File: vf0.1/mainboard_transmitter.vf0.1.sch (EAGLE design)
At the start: 10 parts, among them J1 AUDIO-JACK2PTH, Y1 16MHz

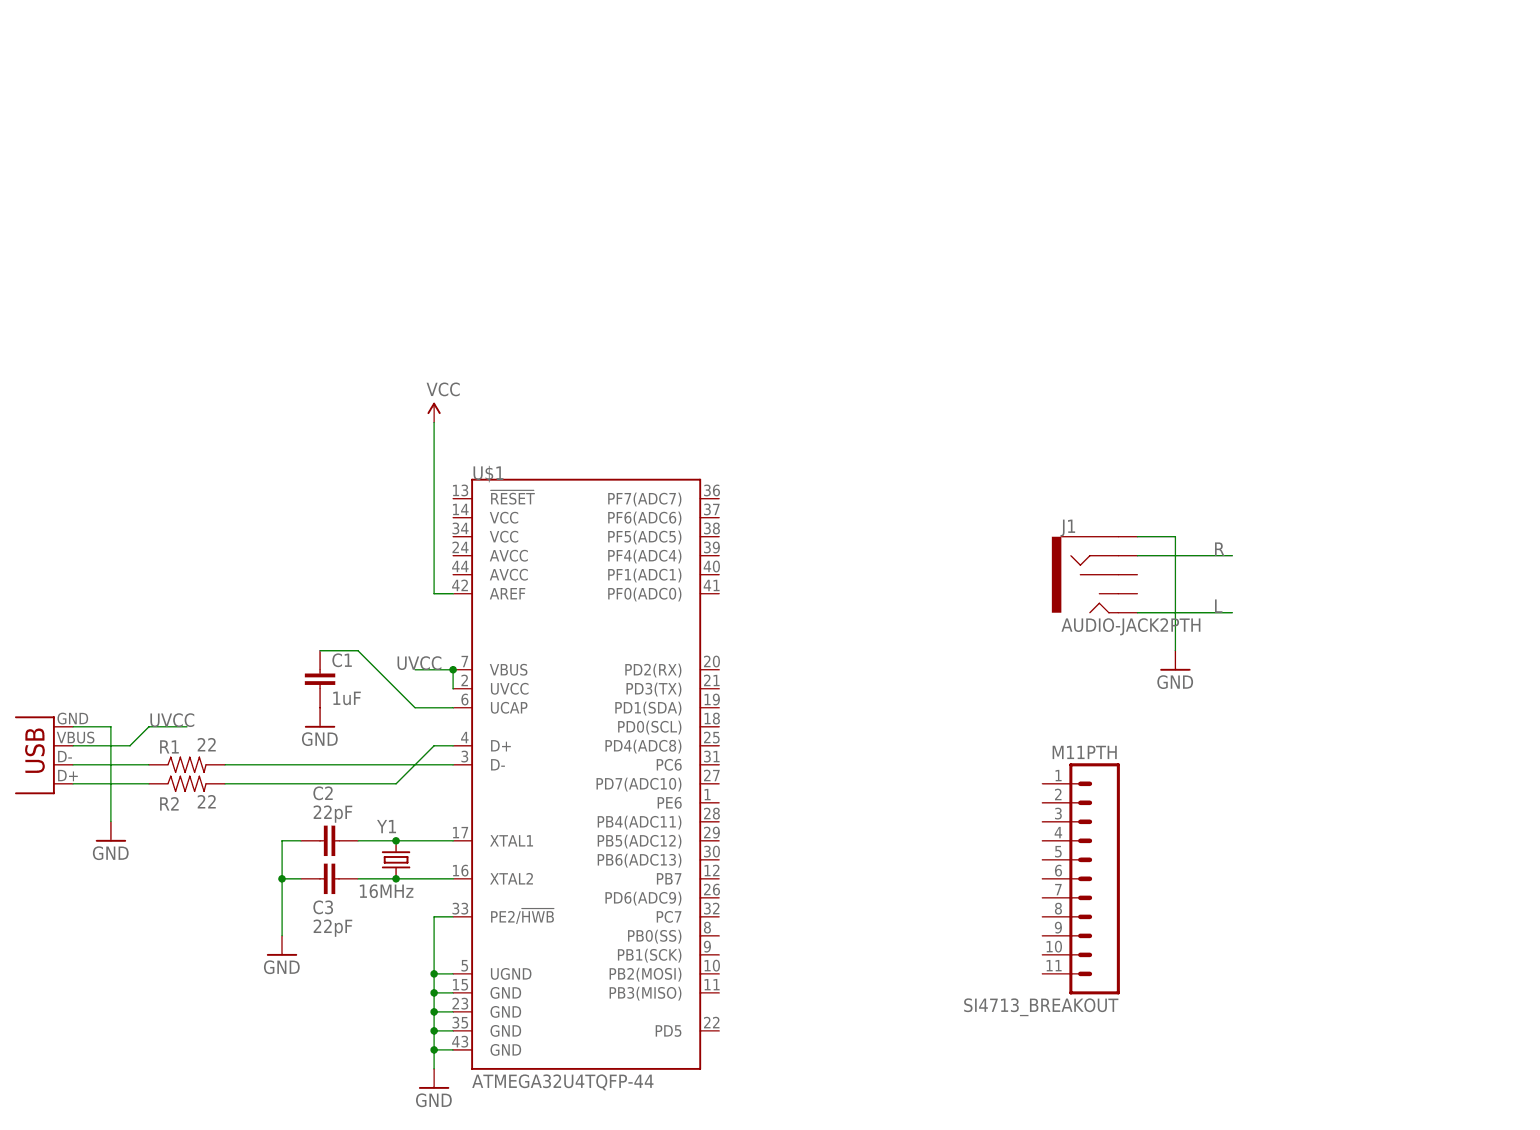
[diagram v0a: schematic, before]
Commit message: Mostly complete, routed audio, FM transmitter, data transmitter
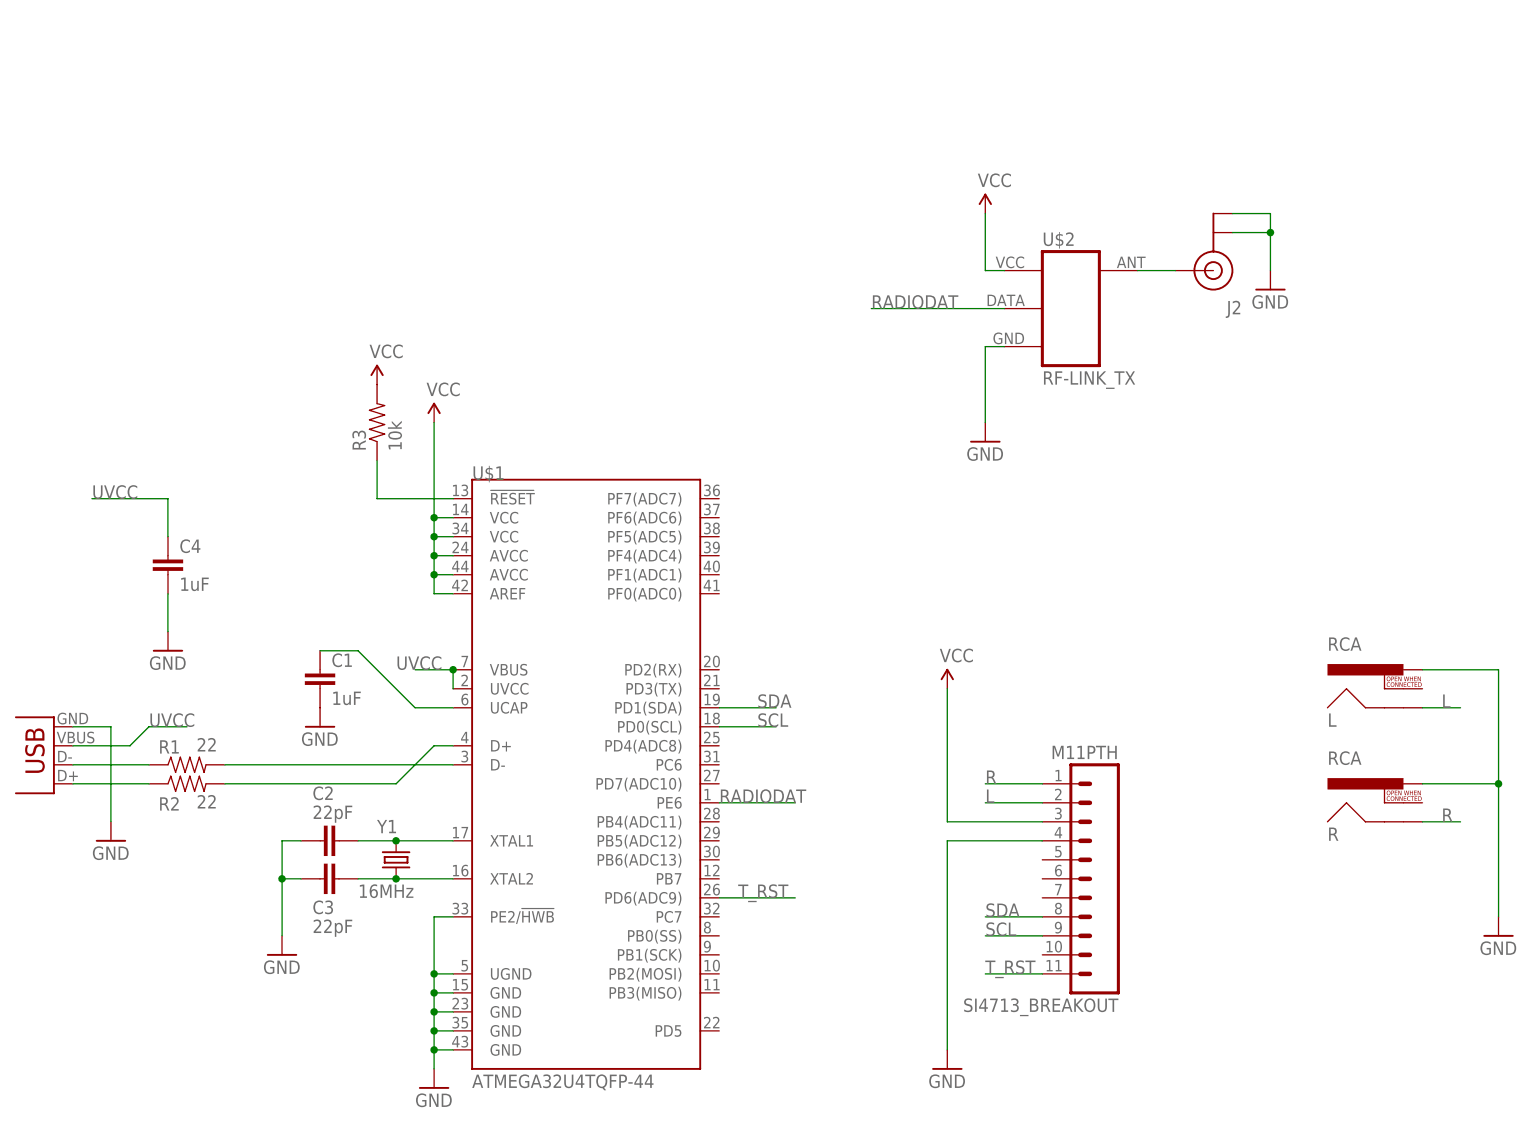
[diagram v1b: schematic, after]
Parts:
- removed J1: AUDIO-JACK2PTH, SparkFun-Connectors:AUDIO-JACK2PTH
- added C4: 1uF, SparkFun-Capacitors:CAPPTH
- added J2: U.FL, SparkFun-Connectors:U.FL
- added L, R: RCA, SparkFun-Connectors:RCA
- added R3: 10k, SparkFun-Resistors:10KOHM-1/4W5%(PTH)VERT
- added U$2: RF-LINK_TX, SparkFun-RF:RF-LINK_TX
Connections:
- new net N$8: R3.1, U$1.!RESET
- new net N$9: J2.SIGNAL, U$2.ANT
- new net RADIODAT: U$1.PE6, U$2.DATA
- new net SCL: SI4713_BREAKOUT.9, U$1.PD0(SCL)
- new net SDA: SI4713_BREAKOUT.8, U$1.PD1(SDA)
- new net T_RST: SI4713_BREAKOUT.11, U$1.PD6(ADC9)
- net GND: now also C4.2, J2.GND@0, J2.GND@1, L.PIN, R.PIN, SI4713_BREAKOUT.4, U$2.GND; no longer J1.SLEEVE
- net L: now also L.SHELL, SI4713_BREAKOUT.2; no longer J1.TIP
- net R: now also R.SHELL, SI4713_BREAKOUT.1; no longer J1.RING
- net UVCC: now also C4.1
- net VCC: now also R3.2, SI4713_BREAKOUT.3, U$1.AVCC@24, U$1.AVCC@44, U$1.VCC@14, U$1.VCC@34, U$2.+5V

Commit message: Final revision of vf0.1
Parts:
- removed J2: U.FL, SparkFun-Connectors:U.FL
- added J$1: SMA_EDGE, SparkFun-Connectors:SMA_EDGE
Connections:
- removed net UVCC: C4.1, JP1.VBUS, U$1.UVCC, U$1.VBUS
- net GND: now also J$1.GND@0, J$1.GND@1, J$1.GND@2, J$1.GND@3; no longer J2.GND@0, J2.GND@1
- net N$9: now also J$1.SIGNAL; no longer J2.SIGNAL
- net VCC: now also C4.1, JP1.VBUS, U$1.UVCC, U$1.VBUS
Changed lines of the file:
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@@
 <part name="R" library="SparkFun-Connectors" deviceset="RCA" device=""/>
 <part name="GND6" library="SparkFun-Aesthetics" deviceset="GND" device=""/>
-<part name="J2" library="SparkFun-Connectors" deviceset="U.FL" device="" value="U.FL"/>
 <part name="GND8" library="SparkFun-Aesthetics" deviceset="GND" device=""/>
 <part name="U$2" library="SparkFun-RF" deviceset="RF-LINK_TX" device=""/>
@@
 <part name="C4" library="SparkFun-Capacitors" deviceset="CAP" device="PTH" value="1uF"/>
 <part name="GND9" library="SparkFun-Aesthetics" deviceset="GND" device=""/>
+<part name="SUPPLY5" library="SparkFun-Aesthetics" deviceset="VCC" device=""/>
+<part name="SUPPLY6" library="SparkFun-Aesthetics" deviceset="VCC" device=""/>
+<part name="SUPPLY7" library="SparkFun-Aesthetics" deviceset="VCC" device=""/>
+<part name="J$1" library="SparkFun-Connectors" deviceset="SMA_EDGE" device=""/>
 </parts>
 <sheets>
@@
 <instance part="R" gate="G$1" x="152.4" y="48.26"/>
 <instance part="GND6" gate="1" x="162.56" y="30.48"/>
-<instance part="J2" gate="G$1" x="124.46" y="119.38" rot="R180"/>
 <instance part="GND8" gate="1" x="132.08" y="116.84"/>
 <instance part="U$2" gate="G$1" x="104.14" y="116.84"/>
@@
 <instance part="C4" gate="G$1" x="-15.24" y="78.74"/>
 <instance part="GND9" gate="1" x="-15.24" y="68.58"/>
+<instance part="SUPPLY5" gate="G$1" x="-20.32" y="58.42"/>
+<instance part="SUPPLY6" gate="G$1" x="-15.24" y="88.9"/>
+<instance part="SUPPLY7" gate="G$1" x="17.78" y="68.58"/>
+<instance part="J$1" gate="1" x="124.46" y="119.38" rot="R180"/>
 </instances>
 <busses>
@@
 </segment>
 <segment>
-<pinref part="J2" gate="G$1" pin="GND@1"/>
 <pinref part="GND8" gate="1" pin="GND"/>
 <wire x1="127" y1="127" x2="132.08" y2="127" width="0.1524" layer="91"/>
 <wire x1="132.08" y1="127" x2="132.08" y2="124.46" width="0.1524" layer="91"/>
-<pinref part="J2" gate="G$1" pin="GND@0"/>
 <wire x1="132.08" y1="124.46" x2="132.08" y2="119.38" width="0.1524" layer="91"/>
 <wire x1="127" y1="124.46" x2="132.08" y2="124.46" width="0.1524" layer="91"/>
 <junction x="132.08" y="124.46"/>
+<pinref part="J$1" gate="1" pin="GND@0"/>
+<pinref part="J$1" gate="1" pin="GND@1"/>
+<pinref part="J$1" gate="1" pin="GND@3"/>
+<wire x1="127" y1="132.08" x2="132.08" y2="132.08" width="0.1524" layer="91"/>
+<wire x1="132.08" y1="132.08" x2="132.08" y2="129.54" width="0.1524" layer="91"/>
+<junction x="132.08" y="127"/>
+<pinref part="J$1" gate="1" pin="GND@2"/>
+<wire x1="132.08" y1="129.54" x2="132.08" y2="127" width="0.1524" layer="91"/>
+<wire x1="127" y1="129.54" x2="132.08" y2="129.54" width="0.1524" layer="91"/>
+<junction x="132.08" y="129.54"/>
 </segment>
 <segment>
@@
 <wire x1="20.32" y1="55.88" x2="22.86" y2="55.88" width="0.1524" layer="91"/>
 <pinref part="U$1" gate="G$1" pin="D+"/>
-</segment>
-</net>
-<net name="UVCC" class="0">
-<segment>
-<pinref part="JP1" gate="G$1" pin="VBUS"/>
-<wire x1="-27.94" y1="55.88" x2="-20.32" y2="55.88" width="0.1524" layer="91"/>
-<wire x1="-20.32" y1="55.88" x2="-17.78" y2="58.42" width="0.1524" layer="91"/>
-<wire x1="-17.78" y1="58.42" x2="-12.7" y2="58.42" width="0.1524" layer="91"/>
-<label x="-17.78" y="58.42" size="1.778" layer="95"/>
-</segment>
-<segment>
-<pinref part="U$1" gate="G$1" pin="UVCC"/>
-<pinref part="U$1" gate="G$1" pin="VBUS"/>
-<wire x1="22.86" y1="66.04" x2="22.86" y2="63.5" width="0.1524" layer="91"/>
-<wire x1="22.86" y1="66.04" x2="17.78" y2="66.04" width="0.1524" layer="91"/>
-<junction x="22.86" y="66.04"/>
-<label x="15.24" y="66.04" size="1.778" layer="95"/>
-</segment>
-<segment>
-<pinref part="C4" gate="G$1" pin="1"/>
-<wire x1="-15.24" y1="83.82" x2="-15.24" y2="88.9" width="0.1524" layer="91"/>
-<wire x1="-15.24" y1="88.9" x2="-25.4" y2="88.9" width="0.1524" layer="91"/>
-<label x="-25.4" y="88.9" size="1.778" layer="95"/>
 </segment>
 </net>
@@
 <net name="N$9" class="0">
 <segment>
-<pinref part="J2" gate="G$1" pin="SIGNAL"/>
 <pinref part="U$2" gate="G$1" pin="ANT"/>
 <wire x1="119.38" y1="119.38" x2="114.3" y2="119.38" width="0.1524" layer="91"/>
+<pinref part="J$1" gate="1" pin="SIGNAL"/>
 </segment>
 </net>
@@
 <pinref part="SUPPLY4" gate="G$1" pin="VCC"/>
 </segment>
+<segment>
+<pinref part="JP1" gate="G$1" pin="VBUS"/>
+<wire x1="-27.94" y1="55.88" x2="-20.32" y2="55.88" width="0.1524" layer="91"/>
+<wire x1="-20.32" y1="55.88" x2="-20.32" y2="58.42" width="0.1524" layer="91"/>
+<pinref part="SUPPLY5" gate="G$1" pin="VCC"/>
+</segment>
+<segment>
+<pinref part="C4" gate="G$1" pin="1"/>
+<wire x1="-15.24" y1="83.82" x2="-15.24" y2="88.9" width="0.1524" layer="91"/>
+<pinref part="SUPPLY6" gate="G$1" pin="VCC"/>
+</segment>
+<segment>
+<pinref part="U$1" gate="G$1" pin="UVCC"/>
+<pinref part="U$1" gate="G$1" pin="VBUS"/>
+<wire x1="22.86" y1="66.04" x2="22.86" y2="63.5" width="0.1524" layer="91"/>
+<wire x1="22.86" y1="66.04" x2="17.78" y2="66.04" width="0.1524" layer="91"/>
+<wire x1="17.78" y1="66.04" x2="17.78" y2="68.58" width="0.1524" layer="91"/>
+<junction x="22.86" y="66.04"/>
+<pinref part="SUPPLY7" gate="G$1" pin="VCC"/>
+</segment>
 </net>
 <net name="RADIODAT" class="0">
@@
 </sheet>
 </sheets>
+<errors>
+</errors>
 </schematic>
 </drawing>

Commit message: Finalized transmitter main board
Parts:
- added J1: AVR_SPI_PRG_6TESTPOINTS, SparkFun-Connectors:AVR_SPI_PRG_6TESTPOINTS
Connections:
- removed net N$8: R3.1, U$1.!RESET
- new net !RESET: J1.5, R3.1, U$1.!RESET
- new net MISO: J1.1, U$1.PB2(MOSI)
- new net MOSI: J1.4, U$1.PB3(MISO)
- new net SCK: J1.3, U$1.PB1(SCK)
- net GND: now also J1.6
- net RADIODAT: now also U$1.PD4(ADC8); no longer U$1.PE6
- net VCC: now also J1.2
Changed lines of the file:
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@@
 <part name="SUPPLY7" library="SparkFun-Aesthetics" deviceset="VCC" device=""/>
 <part name="J$1" library="SparkFun-Connectors" deviceset="SMA_EDGE" device=""/>
+<part name="J1" library="SparkFun-Connectors" deviceset="AVR_SPI_PRG_6" device="TESTPOINTS"/>
+<part name="GND10" library="SparkFun-Aesthetics" deviceset="GND" device=""/>
+<part name="SUPPLY8" library="SparkFun-Aesthetics" deviceset="VCC" device=""/>
 </parts>
 <sheets>
@@
 <instance part="SUPPLY7" gate="G$1" x="17.78" y="68.58"/>
 <instance part="J$1" gate="1" x="124.46" y="119.38" rot="R180"/>
+<instance part="J1" gate="G$1" x="38.1" y="139.7"/>
+<instance part="GND10" gate="1" x="53.34" y="124.46"/>
+<instance part="SUPPLY8" gate="G$1" x="58.42" y="147.32"/>
 </instances>
 <busses>
@@
 <wire x1="-15.24" y1="71.12" x2="-15.24" y2="76.2" width="0.1524" layer="91"/>
 </segment>
+<segment>
+<pinref part="GND10" gate="1" pin="GND"/>
+<wire x1="53.34" y1="137.16" x2="53.34" y2="127" width="0.1524" layer="91"/>
+<pinref part="J1" gate="G$1" pin="6"/>
+<wire x1="48.26" y1="137.16" x2="53.34" y2="137.16" width="0.1524" layer="91"/>
+</segment>
 </net>
 <net name="N$1" class="0">
@@
 <pinref part="SUPPLY7" gate="G$1" pin="VCC"/>
 </segment>
+<segment>
+<pinref part="J1" gate="G$1" pin="2"/>
+<wire x1="48.26" y1="142.24" x2="58.42" y2="142.24" width="0.1524" layer="91"/>
+<wire x1="58.42" y1="142.24" x2="58.42" y2="147.32" width="0.1524" layer="91"/>
+<pinref part="SUPPLY8" gate="G$1" pin="VCC"/>
+</segment>
 </net>
 <net name="RADIODAT" class="0">
@@
 </segment>
 <segment>
-<pinref part="U$1" gate="G$1" pin="PE6"/>
-<wire x1="58.42" y1="48.26" x2="68.58" y2="48.26" width="0.1524" layer="91"/>
-<label x="58.42" y="48.26" size="1.778" layer="95"/>
-</segment>
-</net>
-<net name="N$8" class="0">
+<pinref part="U$1" gate="G$1" pin="PD4(ADC8)"/>
+<wire x1="58.42" y1="55.88" x2="66.04" y2="55.88" width="0.1524" layer="91"/>
+<label x="58.42" y="55.88" size="1.778" layer="95"/>
+</segment>
+</net>
+<net name="!RESET" class="0">
 <segment>
 <pinref part="U$1" gate="G$1" pin="!RESET"/>
@@
 <wire x1="22.86" y1="88.9" x2="12.7" y2="88.9" width="0.1524" layer="91"/>
 <wire x1="12.7" y1="88.9" x2="12.7" y2="93.98" width="0.1524" layer="91"/>
+<label x="12.7" y="88.9" size="1.778" layer="95"/>
+</segment>
+<segment>
+<pinref part="J1" gate="G$1" pin="5"/>
+<wire x1="30.48" y1="137.16" x2="15.24" y2="137.16" width="0.1524" layer="91"/>
+<label x="15.24" y="137.16" size="1.778" layer="95"/>
 </segment>
 </net>
@@
 </segment>
 </net>
+<net name="SCK" class="0">
+<segment>
+<pinref part="J1" gate="G$1" pin="3"/>
+<wire x1="30.48" y1="139.7" x2="15.24" y2="139.7" width="0.1524" layer="91"/>
+<label x="15.24" y="139.7" size="1.778" layer="95"/>
+</segment>
+<segment>
+<pinref part="U$1" gate="G$1" pin="PB1(SCK)"/>
+<wire x1="58.42" y1="27.94" x2="63.5" y2="27.94" width="0.1524" layer="91"/>
+<label x="60.96" y="27.94" size="1.778" layer="95"/>
+</segment>
+</net>
+<net name="MISO" class="0">
+<segment>
+<pinref part="J1" gate="G$1" pin="1"/>
+<wire x1="30.48" y1="142.24" x2="15.24" y2="142.24" width="0.1524" layer="91"/>
+<label x="15.24" y="142.24" size="1.778" layer="95"/>
+</segment>
+<segment>
+<pinref part="U$1" gate="G$1" pin="PB2(MOSI)"/>
+<wire x1="58.42" y1="25.4" x2="63.5" y2="25.4" width="0.1524" layer="91"/>
+<label x="60.96" y="25.4" size="1.778" layer="95"/>
+</segment>
+</net>
+<net name="MOSI" class="0">
+<segment>
+<pinref part="J1" gate="G$1" pin="4"/>
+<wire x1="48.26" y1="139.7" x2="60.96" y2="139.7" width="0.1524" layer="91"/>
+<label x="55.88" y="139.7" size="1.778" layer="95"/>
+</segment>
+<segment>
+<pinref part="U$1" gate="G$1" pin="PB3(MISO)"/>
+<wire x1="58.42" y1="22.86" x2="63.5" y2="22.86" width="0.1524" layer="91"/>
+<label x="60.96" y="22.86" size="1.778" layer="95"/>
+</segment>
+</net>
